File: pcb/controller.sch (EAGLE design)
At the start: 20 parts, among them J2 AVR_SPI_PROG_3X22X3_LOCK, Q1 ECS-160-20-3X-TR, U1 32U4

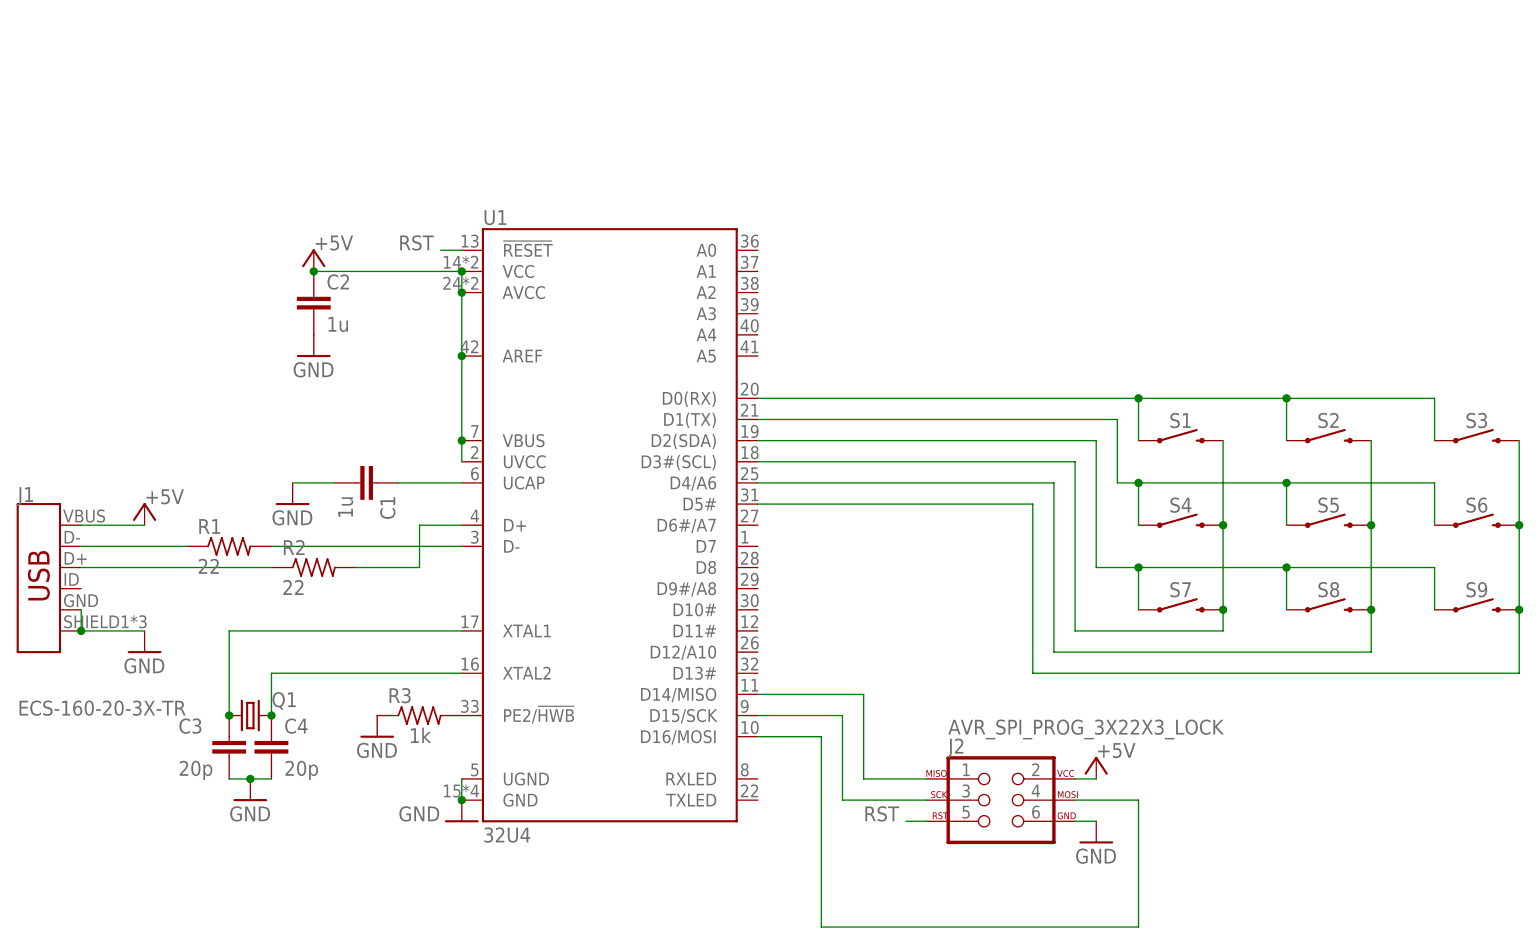
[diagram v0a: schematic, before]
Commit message: change to non-arduino atmega32u4
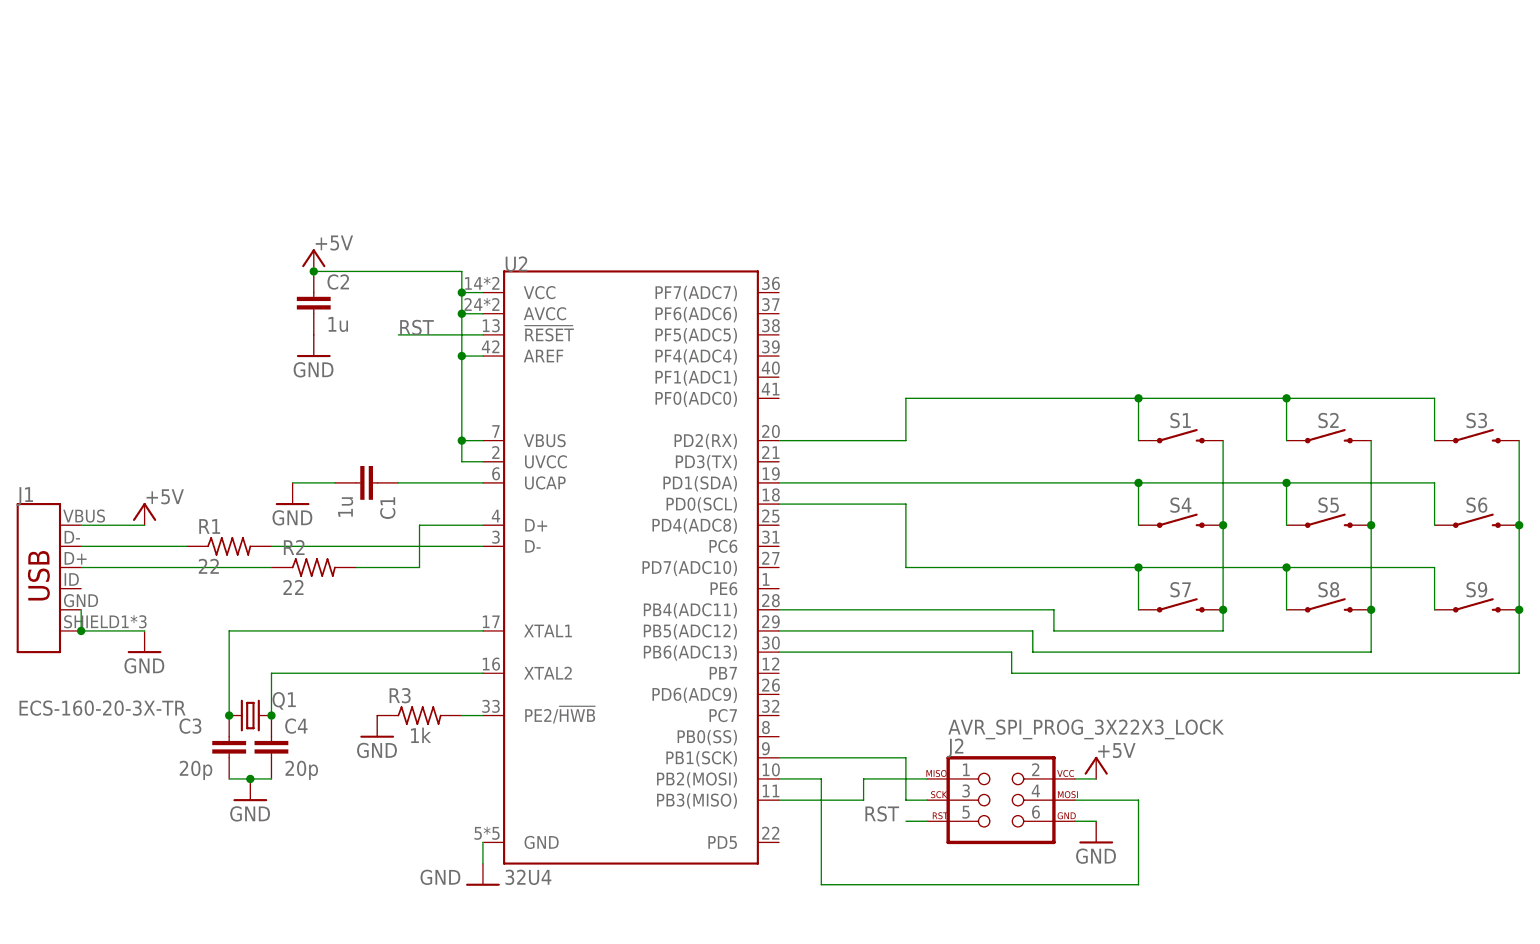
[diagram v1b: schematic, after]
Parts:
- removed U1: 32U4, SparkFun-IC-Microcontroller:ATMEGA32U4-ARDUINOQFN2
- added U2: 32U4, SparkFun-IC-Microcontroller:ATMEGA32U4QFN
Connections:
- net +5V: now also U2.AREF, U2.AVCC@24, U2.UVCC, U2.VBUS, U2.VCC@14; no longer U1.AREF, U1.AVCC, U1.UVCC, U1.VBUS, U1.VCC
- net GND: now also U2.GND; no longer U1.GND, U1.UGND
- net N$1: now also U2.UCAP; no longer U1.UCAP
- net N$10: now also U2.PB1(SCK); no longer U1.D15/SCK
- net N$11: now also U2.PB2(MOSI); no longer U1.D16/MOSI
- net N$12: now also U2.PB4(ADC11); no longer U1.D3#(SCL)
- net N$13: now also U2.PB5(ADC12); no longer U1.D4/A6
- net N$14: now also U2.PD2(RX); no longer U1.D0(RX)
- net N$18: now also U2.PD1(SDA); no longer U1.D1(TX)
- net N$19: now also U2.PB6(ADC13); no longer U1.D5#
- net N$20: now also U2.PD0(SCL); no longer U1.D2(SDA)
- net N$4: now also U2.D+; no longer U1.D+
- net N$5: now also U2.D-; no longer U1.D-
- net N$6: now also U2.PE2/!HWB; no longer U1.PE2/!HWB
- net N$7: now also U2.XTAL2; no longer U1.XTAL2
- net N$8: now also U2.XTAL1; no longer U1.XTAL1
- net N$9: now also U2.PB3(MISO); no longer U1.D14/MISO
- net RST: now also U2.!RESET; no longer U1.!RESET

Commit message: finish controller
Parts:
- removed C2: 1u, rcl:C-EUC0805
- removed C3, C4: 20p, rcl:C-EUC0805
- removed J2: AVR_SPI_PROG_3X22X3_LOCK, SparkFun-Connectors:AVR_SPI_PROG_3X22X3_LOCK
- removed Q1: ECS-160-20-3X-TR, adafruit:CRYSTALHC49UP
- removed S9: MOMENTARY-SWITCH-SPST-SMD-6.0X3.5MM, SparkFun-Switches:MOMENTARY-SWITCH-SPST-SMD-6.0X3.5MM
- removed U2: 32U4, SparkFun-IC-Microcontroller:ATMEGA32U4QFN
- added R4, R5, R6, R7, R8: (no value), rcl:R-US_R0603
- added U$2: JST-ZH-5SMD-RA, josh:JST-ZH-5SMD-RA
- added U1: 74HCT165TSSOP16, josh:74HCT165TSSOP16
- C1: value 1u -> (none); device rcl:C-EUC0805 -> rcl:C-EUC0603
- R1, R2: value 22 -> (none); device rcl:R-US_R0805 -> rcl:R-US_R0603
- R3: value 1k -> (none); device rcl:R-US_R0805 -> rcl:R-US_R0603
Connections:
- removed net N$12: S1.2, S4.2, S7.2, U2.PB4(ADC11)
- removed net N$13: S2.2, S5.2, S8.2, U2.PB5(ADC12)
- removed net N$14: S1.1, S2.1, S3.1, U2.PD2(RX)
- removed net N$18: S4.1, S5.1, S6.1, U2.PD1(SDA)
- removed net N$19: S3.2, S6.2, S9.2, U2.PB6(ADC13)
- removed net N$20: S7.1, S8.1, S9.1, U2.PD0(SCL)
- removed net RST: J2.5, U2.!RESET
- net +5V: now also C1.2, R1.2, R2.2, R3.2, R4.2, R5.2, R6.2, R7.2, R8.2, U$2.1, U1.5V, U1.DS; no longer C2.1, J2.2, U2.AREF, U2.AVCC@24, U2.UVCC, U2.VBUS, U2.VCC@14
- net GND: now also C1.1, S1.1, S2.1, S3.1, S4.1, S5.1, S6.1, S7.1, S8.1, U$2.5, U1.CE', U1.GND; no longer C1.2, C2.2, C3.2, C4.2, J2.6, R3.1, U2.GND
- net N$1: now also U$2.4, U1.CP; no longer C1.1, U2.UCAP
- net N$10: now also R7.1, S7.2, U1.D6; no longer J2.3, U2.PB1(SCK)
- net N$11: now also R8.1, S8.2, U1.D7; no longer J2.4, U2.PB2(MOSI)
- net N$2: now also U$2.3, U1.PL'; no longer J1.D-, R1.1
- net N$3: now also U$2.2, U1.Q7'; no longer J1.D+, R2.1
- net N$4: now also R1.1, S1.2, U1.D0; no longer R2.2, U2.D+
- net N$5: now also R2.1, S2.2, U1.D1; no longer R1.2, U2.D-
- net N$6: now also R3.1, S3.2, U1.D2; no longer R3.2, U2.PE2/!HWB
- net N$7: now also R4.1, S4.2, U1.D3; no longer C4.1, Q1.2, U2.XTAL2
- net N$8: now also R5.1, S5.2, U1.D4; no longer C3.1, Q1.1, U2.XTAL1
- net N$9: now also R6.1, S6.2, U1.D5; no longer J2.1, U2.PB3(MISO)
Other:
- moved on the sheet: C1, R1, R2, R3, S1, S2, S3, S4, S5, S6, S7, S8

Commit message: update resistor values
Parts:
- C1: value (none) -> 100n
- R1, R2, R3, R4, R5, R6, R7, R8: value (none) -> 4.7k
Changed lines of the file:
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@@
 <part name="GND3" library="supply1" library_urn="urn:adsk.eagle:library:371" deviceset="GND" device=""/>
 <part name="GND4" library="supply1" library_urn="urn:adsk.eagle:library:371" deviceset="GND" device=""/>
-<part name="R1" library="rcl" library_urn="urn:adsk.eagle:library:334" deviceset="R-US_" device="R0603" package3d_urn="urn:adsk.eagle:package:23555/3"/>
-<part name="R2" library="rcl" library_urn="urn:adsk.eagle:library:334" deviceset="R-US_" device="R0603" package3d_urn="urn:adsk.eagle:package:23555/3"/>
-<part name="R3" library="rcl" library_urn="urn:adsk.eagle:library:334" deviceset="R-US_" device="R0603" package3d_urn="urn:adsk.eagle:package:23555/3"/>
-<part name="R4" library="rcl" library_urn="urn:adsk.eagle:library:334" deviceset="R-US_" device="R0603" package3d_urn="urn:adsk.eagle:package:23555/3"/>
-<part name="R5" library="rcl" library_urn="urn:adsk.eagle:library:334" deviceset="R-US_" device="R0603" package3d_urn="urn:adsk.eagle:package:23555/3"/>
-<part name="R6" library="rcl" library_urn="urn:adsk.eagle:library:334" deviceset="R-US_" device="R0603" package3d_urn="urn:adsk.eagle:package:23555/3"/>
-<part name="R7" library="rcl" library_urn="urn:adsk.eagle:library:334" deviceset="R-US_" device="R0603" package3d_urn="urn:adsk.eagle:package:23555/3"/>
-<part name="R8" library="rcl" library_urn="urn:adsk.eagle:library:334" deviceset="R-US_" device="R0603" package3d_urn="urn:adsk.eagle:package:23555/3"/>
+<part name="R1" library="rcl" library_urn="urn:adsk.eagle:library:334" deviceset="R-US_" device="R0603" package3d_urn="urn:adsk.eagle:package:23555/3" value="4.7k"/>
+<part name="R2" library="rcl" library_urn="urn:adsk.eagle:library:334" deviceset="R-US_" device="R0603" package3d_urn="urn:adsk.eagle:package:23555/3" value="4.7k"/>
+<part name="R3" library="rcl" library_urn="urn:adsk.eagle:library:334" deviceset="R-US_" device="R0603" package3d_urn="urn:adsk.eagle:package:23555/3" value="4.7k"/>
+<part name="R4" library="rcl" library_urn="urn:adsk.eagle:library:334" deviceset="R-US_" device="R0603" package3d_urn="urn:adsk.eagle:package:23555/3" value="4.7k"/>
+<part name="R5" library="rcl" library_urn="urn:adsk.eagle:library:334" deviceset="R-US_" device="R0603" package3d_urn="urn:adsk.eagle:package:23555/3" value="4.7k"/>
+<part name="R6" library="rcl" library_urn="urn:adsk.eagle:library:334" deviceset="R-US_" device="R0603" package3d_urn="urn:adsk.eagle:package:23555/3" value="4.7k"/>
+<part name="R7" library="rcl" library_urn="urn:adsk.eagle:library:334" deviceset="R-US_" device="R0603" package3d_urn="urn:adsk.eagle:package:23555/3" value="4.7k"/>
+<part name="R8" library="rcl" library_urn="urn:adsk.eagle:library:334" deviceset="R-US_" device="R0603" package3d_urn="urn:adsk.eagle:package:23555/3" value="4.7k"/>
 <part name="P+3" library="supply1" library_urn="urn:adsk.eagle:library:371" deviceset="+5V" device=""/>
 <part name="S1" library="SparkFun-Switches" deviceset="MOMENTARY-SWITCH-SPST" device="-SMD-6.0X3.5MM"/>
@@
 <part name="P+4" library="supply1" library_urn="urn:adsk.eagle:library:371" deviceset="+5V" device=""/>
 <part name="P+5" library="supply1" library_urn="urn:adsk.eagle:library:371" deviceset="+5V" device=""/>
-<part name="C1" library="rcl" library_urn="urn:adsk.eagle:library:334" deviceset="C-EU" device="C0603" package3d_urn="urn:adsk.eagle:package:23616/2"/>
+<part name="C1" library="rcl" library_urn="urn:adsk.eagle:library:334" deviceset="C-EU" device="C0603" package3d_urn="urn:adsk.eagle:package:23616/2" value="100n"/>
 <part name="P+6" library="supply1" library_urn="urn:adsk.eagle:library:371" deviceset="+5V" device=""/>
 <part name="GND6" library="supply1" library_urn="urn:adsk.eagle:library:371" deviceset="GND" device=""/>
@@
 <attribute name="VALUE" x="39.37" y="20.32" size="1.778" layer="96" rot="MR0"/>
 </instance>
-<instance part="P+2" gate="1" x="35.56" y="38.1" smashed="yes">
-<attribute name="VALUE" x="33.02" y="33.02" size="1.778" layer="96" rot="R90"/>
-</instance>
-<instance part="GND2" gate="1" x="35.56" y="22.86" smashed="yes">
-<attribute name="VALUE" x="33.02" y="20.32" size="1.778" layer="96"/>
+<instance part="P+2" gate="1" x="45.72" y="38.1" smashed="yes">
+<attribute name="VALUE" x="45.72" y="38.1" size="1.778" layer="96"/>
+</instance>
+<instance part="GND2" gate="1" x="45.72" y="22.86" smashed="yes">
+<attribute name="VALUE" x="43.18" y="20.32" size="1.778" layer="96"/>
 </instance>
 <instance part="GND3" gate="1" x="76.2" y="35.56" smashed="yes">
@@
 </instance>
 <instance part="P+6" gate="1" x="93.98" y="73.66" smashed="yes">
-<attribute name="VALUE" x="91.44" y="68.58" size="1.778" layer="96" rot="R90"/>
+<attribute name="VALUE" x="93.98" y="73.66" size="1.778" layer="96"/>
 </instance>
 <instance part="GND6" gate="1" x="93.98" y="60.96" smashed="yes">
@@
 <pinref part="U$2" gate="G$1" pin="1"/>
 <pinref part="P+2" gate="1" pin="+5V"/>
+<wire x1="45.72" y1="35.56" x2="35.56" y2="35.56" width="0.1524" layer="91"/>
 </segment>
 <segment>
@@
 <pinref part="U$2" gate="G$1" pin="5"/>
 <pinref part="GND2" gate="1" pin="GND"/>
-</segment>
-<segment>
+<wire x1="45.72" y1="25.4" x2="35.56" y2="25.4" width="0.1524" layer="91"/>
+</segment>
+<segment>

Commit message: update values and name placement
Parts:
- renumbered U$2 to J2
